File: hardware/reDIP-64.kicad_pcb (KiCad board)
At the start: 6 copper layers, 25.4 x 50.8 mm, 129 parts, among them J1 USB_C_Receptacle, J2 Conn_02x05_Odd_Even, J3 Conn_01x20, J4 Conn_01x20, J5 Conn_01x20, J6 Conn_01x20, J7 Conn_01x20, Q1 PDTA143ZMB, SW1 KXT331LHS, U1 FPF1048, U10 PTN5110, U11 FUSB340, U12 DSC1103CE2-135.0000, U13 FSA2259, U14 W957A8MFYA5I, U15 W25Q128JVPIM, U16 SN74CBTD16211DGVR, U17 SN74CBTD16211DGVR, U18 SN74CBTD16211DGVR, U19 SN74CBTD16211DGVR, U2 NCP163AMX250TBG, U3 MYRGP330100W21RA, U4 FPF2195, U5 NCP163AMX120TBG, U6 MYRGP120100W21RA, U7 NCP163AMX300TBG, U8 LFE5UM5G-25F-8MG285C, U9 SGTL5000XNLA3

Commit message: Various improvements
* Removed slash from sheet names
* Reannotated schematics
* Example derivation of clocks in schematics
* Identical capacitors for DisplayPort main lanes and AUX
* Replaced switch FSA2259UMX with FSUSB42UMX
* Modified PCB physical stackup to (hopefully) be manufacturable
* Only one microvia size (0.1mm)
* Changed track width for differential pairs
* Routing cleanups and improvements
* Added files for manufacture
* Updated README

Many thanks for advice and help go to @azonenberg, @DX-MON, @gatecat,
@smunaut, and @zyp.
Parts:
- removed the U13 at (108.8, 103.0)
- added U2: FSUSB42UMX, ONSemi:CASE523BC_1.4x1.8_P0.4mm, B.Cu at (108.8, 103.0)
- C1: renamed from C43; value 0.1uF -> 100nF
- C2: renamed from C45; value 0.1uF -> 100nF
- C3: renamed from C46; value 0.1uF -> 100nF
- C4: renamed from C47; value 0.1uF -> 100nF
- C5: renamed from C48; value 150nF -> 100nF
- C6: renamed from C49; value 150nF -> 100nF
- U3: renamed from U10; value PTN5110 -> PTN5110DHQ
- renumbered C41 to C10, C44 to C11, C7 to C12, C5 to C13, C21 to C14, C22 to C15, C23 to C16, C24 to C17, C6 to C18, C8 to C19, C25 to C20, C13 to C21, C26 to C22, C14 to C23, C27 to C24, C15 to C25, C28 to C26, C16 to C27, C17 to C28, C18 to C30, C30 to C31, C1 to C32, C9 to C33, C2 to C34, C10 to C35, C11 to C36, C3 to C37, C19 to C38, C12 to C39, C4 to C40, C20 to C41, C58 to C42, C62 to C43, C59 to C44, C63 to C45, C60 to C46, C64 to C47, C61 to C48, C65 to C49, C56 to C50, C66 to C51, C57 to C52, C67 to C53, C52 to C55, C55 to C56, C53 to C57, C50 to C58, C51 to C59, C31 to C60, C34 to C61, C35 to C62, C36 to C63, C32 to C64, C33 to C65, C37 to C66, C38 to C67, C42 to C7, C39 to C8, C40 to C9, D2 to D1, D3 to D2, D4 to D3, D1 to D4, FB3 to FB2, FB2 to FB3, J3 to J2, J6 to J3, J5 to J4, J7 to J5, J4 to J6, J2 to J7, R6 to R1, R13 to R10, R9 to R11, R14 to R12, R2 to R13, R3 to R14, R1 to R15, R21 to R17, R17 to R18, R22 to R19, R7 to R2, R19 to R20, R20 to R21, R18 to R22, R8 to R3, R10 to R4, R11 to R5, R4 to R6, R5 to R7, R12 to R8, R15 to R9, U11 to U1, U5 to U10, U2 to U11, U7 to U12, U16 to U13, U18 to U14, U17 to U15, U19 to U16, U14 to U17, U15 to U18, U9 to U19, U8 to U4, U12 to U5, U1 to U6, U4 to U7, U3 to U8, U6 to U9
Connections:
- net /Config / Memory/FLASH_~CS~ renamed /Config_Memory/FLASH_~CS~
- net /Config / Memory/LED renamed /Config_Memory/LED
- net /Config / Memory/MEM_CLK renamed /Config_Memory/MEM_CLK
- net /Config / Memory/MEM_IO0 renamed /Config_Memory/MEM_IO0
- net /Config / Memory/MEM_IO1 renamed /Config_Memory/MEM_IO1
- net /Config / Memory/MEM_IO2 renamed /Config_Memory/MEM_IO2
- net /Config / Memory/MEM_IO3 renamed /Config_Memory/MEM_IO3
- net /Config / Memory/MEM_IO4 renamed /Config_Memory/MEM_IO4
- net /Config / Memory/MEM_IO5 renamed /Config_Memory/MEM_IO5
- net /Config / Memory/MEM_IO6 renamed /Config_Memory/MEM_IO6
- net /Config / Memory/MEM_IO7 renamed /Config_Memory/MEM_IO7
- net /Config / Memory/RAM_~CS~ renamed /Config_Memory/RAM_~CS~
- net /Config / Memory/RWDS renamed /Config_Memory/RWDS
- net /Config / Memory/TCK renamed /Config_Memory/TCK
- net /Config / Memory/TDI renamed /Config_Memory/TDI
- net /Config / Memory/TDO renamed /Config_Memory/TDO
- net /Config / Memory/TMS renamed /Config_Memory/TMS
- net /Config / Memory/~BOOT~ renamed /Config_Memory/~BOOT~
- net /Config / Memory/~BTN~ renamed /Config_Memory/~BTN~
- net /FPGA / IO/A0 renamed /FPGA_IO/A0
- net /FPGA / IO/A1 renamed /FPGA_IO/A1
- net /FPGA / IO/A10 renamed /FPGA_IO/A10
- net /FPGA / IO/A11 renamed /FPGA_IO/A11
- net /FPGA / IO/A12 renamed /FPGA_IO/A12
- net /FPGA / IO/A13 renamed /FPGA_IO/A13
- net /FPGA / IO/A14 renamed /FPGA_IO/A14
- net /FPGA / IO/A15 renamed /FPGA_IO/A15
- net /FPGA / IO/A2 renamed /FPGA_IO/A2
- net /FPGA / IO/A3 renamed /FPGA_IO/A3
- net /FPGA / IO/A4 renamed /FPGA_IO/A4
- net /FPGA / IO/A5 renamed /FPGA_IO/A5
- net /FPGA / IO/A6 renamed /FPGA_IO/A6
- net /FPGA / IO/A7 renamed /FPGA_IO/A7
- net /FPGA / IO/A8 renamed /FPGA_IO/A8
- net /FPGA / IO/A9 renamed /FPGA_IO/A9
- net /FPGA / IO/AEC renamed /FPGA_IO/AEC
- net /FPGA / IO/BA renamed /FPGA_IO/BA
- net /FPGA / IO/CIA1_CNT renamed /FPGA_IO/CIA1_CNT
- net /FPGA / IO/CIA1_PA0 renamed /FPGA_IO/CIA1_PA0
- net /FPGA / IO/CIA1_PA1 renamed /FPGA_IO/CIA1_PA1
- net /FPGA / IO/CIA1_PA2 renamed /FPGA_IO/CIA1_PA2
- net /FPGA / IO/CIA1_PA3 renamed /FPGA_IO/CIA1_PA3
- net /FPGA / IO/CIA1_PA4 renamed /FPGA_IO/CIA1_PA4
- net /FPGA / IO/CIA1_PA5 renamed /FPGA_IO/CIA1_PA5
- net /FPGA / IO/CIA1_PA6 renamed /FPGA_IO/CIA1_PA6
- net /FPGA / IO/CIA1_PA7 renamed /FPGA_IO/CIA1_PA7
- net /FPGA / IO/CIA1_PB0 renamed /FPGA_IO/CIA1_PB0
- net /FPGA / IO/CIA1_PB1 renamed /FPGA_IO/CIA1_PB1
- net /FPGA / IO/CIA1_PB2 renamed /FPGA_IO/CIA1_PB2
- net /FPGA / IO/CIA1_PB3 renamed /FPGA_IO/CIA1_PB3
- net /FPGA / IO/CIA1_PB4 renamed /FPGA_IO/CIA1_PB4
- net /FPGA / IO/CIA1_PB5 renamed /FPGA_IO/CIA1_PB5
- net /FPGA / IO/CIA1_PB6 renamed /FPGA_IO/CIA1_PB6
- net /FPGA / IO/CIA1_PB7 renamed /FPGA_IO/CIA1_PB7
- net /FPGA / IO/CIA1_SP renamed /FPGA_IO/CIA1_SP
- net /FPGA / IO/CIA1_~FLAG~ renamed /FPGA_IO/CIA1_~FLAG~
- net /FPGA / IO/CIA1_~PC~_TOD renamed /FPGA_IO/CIA1_~PC~_TOD
- net /FPGA / IO/CIA2_CNT renamed /FPGA_IO/CIA2_CNT
- net /FPGA / IO/CIA2_PA0 renamed /FPGA_IO/CIA2_PA0
- net /FPGA / IO/CIA2_PA1 renamed /FPGA_IO/CIA2_PA1
- net /FPGA / IO/CIA2_PA2 renamed /FPGA_IO/CIA2_PA2
- net /FPGA / IO/CIA2_PA3 renamed /FPGA_IO/CIA2_PA3
- net /FPGA / IO/CIA2_PA4 renamed /FPGA_IO/CIA2_PA4
- net /FPGA / IO/CIA2_PA5 renamed /FPGA_IO/CIA2_PA5
- net /FPGA / IO/CIA2_PA6 renamed /FPGA_IO/CIA2_PA6
- net /FPGA / IO/CIA2_PA7 renamed /FPGA_IO/CIA2_PA7
- net /FPGA / IO/CIA2_PB0 renamed /FPGA_IO/CIA2_PB0
- net /FPGA / IO/CIA2_PB1 renamed /FPGA_IO/CIA2_PB1
- net /FPGA / IO/CIA2_PB2 renamed /FPGA_IO/CIA2_PB2
- net /FPGA / IO/CIA2_PB3 renamed /FPGA_IO/CIA2_PB3
- net /FPGA / IO/CIA2_PB4 renamed /FPGA_IO/CIA2_PB4
- net /FPGA / IO/CIA2_PB5 renamed /FPGA_IO/CIA2_PB5
- net /FPGA / IO/CIA2_PB6 renamed /FPGA_IO/CIA2_PB6
- net /FPGA / IO/CIA2_PB7 renamed /FPGA_IO/CIA2_PB7
- net /FPGA / IO/CIA2_SP renamed /FPGA_IO/CIA2_SP
- net /FPGA / IO/CIA2_~FLAG~ renamed /FPGA_IO/CIA2_~FLAG~
- net /FPGA / IO/CIA2_~PC~ renamed /FPGA_IO/CIA2_~PC~
- net /FPGA / IO/COLOR renamed /FPGA_IO/COLOR
- net /FPGA / IO/D0 renamed /FPGA_IO/D0
- net /FPGA / IO/D1 renamed /FPGA_IO/D1
- net /FPGA / IO/D2 renamed /FPGA_IO/D2
- net /FPGA / IO/D3 renamed /FPGA_IO/D3
- net /FPGA / IO/D4 renamed /FPGA_IO/D4
- net /FPGA / IO/D5 renamed /FPGA_IO/D5
- net /FPGA / IO/D6 renamed /FPGA_IO/D6
- net /FPGA / IO/D7 renamed /FPGA_IO/D7
- net /FPGA / IO/DOT_CLOCK renamed /FPGA_IO/DOT_CLOCK
- net /FPGA / IO/DP_AUX+ renamed /FPGA_IO/DP_AUX+
- net /FPGA / IO/DP_AUX- renamed /FPGA_IO/DP_AUX-
- net /FPGA / IO/I1_CNT renamed /FPGA_IO/I1_CNT
- net /FPGA / IO/I1_PA0 renamed /FPGA_IO/I1_PA0
- net /FPGA / IO/I1_PA1 renamed /FPGA_IO/I1_PA1
- net /FPGA / IO/I1_PA2 renamed /FPGA_IO/I1_PA2
- net /FPGA / IO/I1_PA3 renamed /FPGA_IO/I1_PA3
- net /FPGA / IO/I1_PA4 renamed /FPGA_IO/I1_PA4
- net /FPGA / IO/I1_PA5 renamed /FPGA_IO/I1_PA5
- net /FPGA / IO/I1_PA6 renamed /FPGA_IO/I1_PA6
- net /FPGA / IO/I1_PA7 renamed /FPGA_IO/I1_PA7
- net /FPGA / IO/I1_PB0 renamed /FPGA_IO/I1_PB0
- net /FPGA / IO/I1_PB1 renamed /FPGA_IO/I1_PB1
- net /FPGA / IO/I1_PB2 renamed /FPGA_IO/I1_PB2
- net /FPGA / IO/I1_PB3 renamed /FPGA_IO/I1_PB3
- net /FPGA / IO/I1_PB4 renamed /FPGA_IO/I1_PB4
- net /FPGA / IO/I1_PB5 renamed /FPGA_IO/I1_PB5
- net /FPGA / IO/I1_PB6 renamed /FPGA_IO/I1_PB6
- net /FPGA / IO/I1_PB7 renamed /FPGA_IO/I1_PB7
- net /FPGA / IO/I1_SP renamed /FPGA_IO/I1_SP
- net /FPGA / IO/I1_~FLAG~ renamed /FPGA_IO/I1_~FLAG~
- net /FPGA / IO/I1_~PC~_TOD renamed /FPGA_IO/I1_~PC~_TOD
- net /FPGA / IO/I2_CNT renamed /FPGA_IO/I2_CNT
- net /FPGA / IO/I2_PA0 renamed /FPGA_IO/I2_PA0
- net /FPGA / IO/I2_PA1 renamed /FPGA_IO/I2_PA1
- net /FPGA / IO/I2_PA2 renamed /FPGA_IO/I2_PA2
- net /FPGA / IO/I2_PA3 renamed /FPGA_IO/I2_PA3
- net /FPGA / IO/I2_PA4 renamed /FPGA_IO/I2_PA4
- net /FPGA / IO/I2_PA5 renamed /FPGA_IO/I2_PA5
- net /FPGA / IO/I2_PA6 renamed /FPGA_IO/I2_PA6
- net /FPGA / IO/I2_PA7 renamed /FPGA_IO/I2_PA7
- net /FPGA / IO/I2_PB0 renamed /FPGA_IO/I2_PB0
- net /FPGA / IO/I2_PB1 renamed /FPGA_IO/I2_PB1
- net /FPGA / IO/I2_PB2 renamed /FPGA_IO/I2_PB2
- net /FPGA / IO/I2_PB3 renamed /FPGA_IO/I2_PB3
- net /FPGA / IO/I2_PB4 renamed /FPGA_IO/I2_PB4
- net /FPGA / IO/I2_PB5 renamed /FPGA_IO/I2_PB5
- net /FPGA / IO/I2_PB6 renamed /FPGA_IO/I2_PB6
- net /FPGA / IO/I2_PB7 renamed /FPGA_IO/I2_PB7
- net /FPGA / IO/I2_SP renamed /FPGA_IO/I2_SP
- net /FPGA / IO/I2_~FLAG~ renamed /FPGA_IO/I2_~FLAG~
- net /FPGA / IO/I2_~PC~ renamed /FPGA_IO/I2_~PC~
- net /FPGA / IO/I_A0 renamed /FPGA_IO/I_A0
- net /FPGA / IO/I_A1 renamed /FPGA_IO/I_A1
- net /FPGA / IO/I_A10 renamed /FPGA_IO/I_A10
- net /FPGA / IO/I_A11 renamed /FPGA_IO/I_A11
- net /FPGA / IO/I_A12 renamed /FPGA_IO/I_A12
- net /FPGA / IO/I_A13 renamed /FPGA_IO/I_A13
- net /FPGA / IO/I_A14 renamed /FPGA_IO/I_A14
- net /FPGA / IO/I_A15 renamed /FPGA_IO/I_A15
- net /FPGA / IO/I_A2 renamed /FPGA_IO/I_A2
- net /FPGA / IO/I_A3 renamed /FPGA_IO/I_A3
- net /FPGA / IO/I_A4 renamed /FPGA_IO/I_A4
- net /FPGA / IO/I_A5 renamed /FPGA_IO/I_A5
- net /FPGA / IO/I_A6 renamed /FPGA_IO/I_A6
- net /FPGA / IO/I_A7 renamed /FPGA_IO/I_A7
- net /FPGA / IO/I_A8 renamed /FPGA_IO/I_A8
- net /FPGA / IO/I_A9 renamed /FPGA_IO/I_A9
- net /FPGA / IO/I_AEC renamed /FPGA_IO/I_AEC
- net /FPGA / IO/I_BA renamed /FPGA_IO/I_BA
- net /FPGA / IO/I_COLOR renamed /FPGA_IO/I_COLOR
- net /FPGA / IO/I_D0 renamed /FPGA_IO/I_D0
- net /FPGA / IO/I_D1 renamed /FPGA_IO/I_D1
- net /FPGA / IO/I_D2 renamed /FPGA_IO/I_D2
- net /FPGA / IO/I_D3 renamed /FPGA_IO/I_D3
- net /FPGA / IO/I_D4 renamed /FPGA_IO/I_D4
- net /FPGA / IO/I_D5 renamed /FPGA_IO/I_D5
- net /FPGA / IO/I_D6 renamed /FPGA_IO/I_D6
- net /FPGA / IO/I_D7 renamed /FPGA_IO/I_D7
- net /FPGA / IO/I_DOT_CLOCK renamed /FPGA_IO/I_DOT_CLOCK
- net /FPGA / IO/I_P0 renamed /FPGA_IO/I_P0
- net /FPGA / IO/I_P1 renamed /FPGA_IO/I_P1
- net /FPGA / IO/I_P2 renamed /FPGA_IO/I_P2
- net /FPGA / IO/I_P3 renamed /FPGA_IO/I_P3
- net /FPGA / IO/I_P4 renamed /FPGA_IO/I_P4
- net /FPGA / IO/I_P5 renamed /FPGA_IO/I_P5
- net /FPGA / IO/I_POT_X renamed /FPGA_IO/I_POT_X
- net /FPGA / IO/I_POT_Y renamed /FPGA_IO/I_POT_Y
- net /FPGA / IO/I_RDY renamed /FPGA_IO/I_RDY
- net /FPGA / IO/I_R_W renamed /FPGA_IO/I_R_W
- net /FPGA / IO/I_SYNC_LUM renamed /FPGA_IO/I_SYNC_LUM
- net /FPGA / IO/I_~DMA~ renamed /FPGA_IO/I_~DMA~
- net /FPGA / IO/I_~EXROM~ renamed /FPGA_IO/I_~EXROM~
- net /FPGA / IO/I_~GAME~ renamed /FPGA_IO/I_~GAME~
- net /FPGA / IO/I_~IO1~ renamed /FPGA_IO/I_~IO1~
- net /FPGA / IO/I_~IO2~ renamed /FPGA_IO/I_~IO2~
- net /FPGA / IO/I_~IRQ~ renamed /FPGA_IO/I_~IRQ~
- net /FPGA / IO/I_~MENU~ renamed /FPGA_IO/I_~MENU~
- net /FPGA / IO/I_~NMI~ renamed /FPGA_IO/I_~NMI~
- net /FPGA / IO/I_~RES~ renamed /FPGA_IO/I_~RES~
- net /FPGA / IO/I_~ROMH~ renamed /FPGA_IO/I_~ROMH~
- net /FPGA / IO/I_~ROML~ renamed /FPGA_IO/I_~ROML~
- net /FPGA / IO/I_Ø1_IN renamed /FPGA_IO/I_Ø1_IN
- net /FPGA / IO/I_Ø2_OUT renamed /FPGA_IO/I_Ø2_OUT
- net /FPGA / IO/P0 renamed /FPGA_IO/P0
- net /FPGA / IO/P1 renamed /FPGA_IO/P1
- net /FPGA / IO/P2 renamed /FPGA_IO/P2
- net /FPGA / IO/P3 renamed /FPGA_IO/P3
- net /FPGA / IO/P4 renamed /FPGA_IO/P4
- net /FPGA / IO/P5 renamed /FPGA_IO/P5
- net /FPGA / IO/POT_X renamed /FPGA_IO/POT_X
- net /FPGA / IO/POT_Y renamed /FPGA_IO/POT_Y
- net /FPGA / IO/RDY renamed /FPGA_IO/RDY
- net /FPGA / IO/R_W renamed /FPGA_IO/R_W
- net /FPGA / IO/SYNC_LUM renamed /FPGA_IO/SYNC_LUM
- net /FPGA / IO/USB_D+ renamed /FPGA_IO/USB_D+
- net /FPGA / IO/USB_D- renamed /FPGA_IO/USB_D-
- net /FPGA / IO/~ALERT~ renamed /FPGA_IO/~ALERT~
- net /FPGA / IO/~DMA~ renamed /FPGA_IO/~DMA~
- net /FPGA / IO/~EXROM~ renamed /FPGA_IO/~EXROM~
- net /FPGA / IO/~GAME~ renamed /FPGA_IO/~GAME~
- net /FPGA / IO/~IO1~ renamed /FPGA_IO/~IO1~
- net /FPGA / IO/~IO2~ renamed /FPGA_IO/~IO2~
- net /FPGA / IO/~IRQ~ renamed /FPGA_IO/~IRQ~
- net /FPGA / IO/~MENU~ renamed /FPGA_IO/~MENU~
- net /FPGA / IO/~NMI~ renamed /FPGA_IO/~NMI~
- net /FPGA / IO/~RES~ renamed /FPGA_IO/~RES~
- net /FPGA / IO/~ROMH~ renamed /FPGA_IO/~ROMH~
- net /FPGA / IO/~ROML~ renamed /FPGA_IO/~ROML~
- net /FPGA / IO/Ø1_IN renamed /FPGA_IO/Ø1_IN
- net /FPGA / IO/Ø2_OUT renamed /FPGA_IO/Ø2_OUT
- net /USB / DP/AUX+ renamed /USB_DisplayPort/AUX+
- net /USB / DP/AUX- renamed /USB_DisplayPort/AUX-
- net /USB / DP/CC1 renamed /USB_DisplayPort/CC1
- net /USB / DP/CC2 renamed /USB_DisplayPort/CC2
- net /USB / DP/CLK+ renamed /USB_DisplayPort/CLK+
- net /USB / DP/CLK- renamed /USB_DisplayPort/CLK-
- net /USB / DP/D+ renamed /USB_DisplayPort/D+
- net /USB / DP/D- renamed /USB_DisplayPort/D-
- net /USB / DP/DP0+ renamed /USB_DisplayPort/ML0+
- net /USB / DP/DP0- renamed /USB_DisplayPort/ML0-
- net /USB / DP/DP1+ renamed /USB_DisplayPort/ML1+
- net /USB / DP/DP1- renamed /USB_DisplayPort/ML1-
- net /USB / DP/RX+ renamed /USB_DisplayPort/RX+
- net /USB / DP/RX- renamed /USB_DisplayPort/RX-
- net /USB / DP/RX1+ renamed /USB_DisplayPort/RX1+
- net /USB / DP/RX1- renamed /USB_DisplayPort/RX1-
- net /USB / DP/RX2+ renamed /USB_DisplayPort/RX2+
- net /USB / DP/RX2- renamed /USB_DisplayPort/RX2-
- net /USB / DP/SBU1 renamed /USB_DisplayPort/SBU1
- net /USB / DP/SBU2 renamed /USB_DisplayPort/SBU2
- net /USB / DP/TX+ renamed /USB_DisplayPort/TX+
- net /USB / DP/TX- renamed /USB_DisplayPort/TX-
- net /USB / DP/TX1+ renamed /USB_DisplayPort/TX1+
- net /USB / DP/TX1- renamed /USB_DisplayPort/TX1-
- net /USB / DP/TX2+ renamed /USB_DisplayPort/TX2+
- net /USB / DP/TX2- renamed /USB_DisplayPort/TX2-
- net /USB / DP/USB_LINK renamed /USB_DisplayPort/USB_LINK
- net /USB / DP/USB_~CONN~ renamed /USB_DisplayPort/USB_~CONN~
- net /USB / DP/USB_~FLIP~ renamed /USB_DisplayPort/USB_~FLIP~
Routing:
- net GND: track 154.5 -> 160.7 mm, vias 231 -> 236
- net /USB_DisplayPort/SBU2: track 10.6 -> 6.06 mm, vias 4 -> 3
- net /USB_DisplayPort/USB_~FLIP~: track 17.2 -> 14.4 mm, vias 7 -> 6
- net /USB_DisplayPort/AUX-: track 31.3 -> 29.5 mm
- net /USB_DisplayPort/CC2: track 12.1 -> 10.4 mm
- net /USB_DisplayPort/SBU1: track 6.27 -> 4.72 mm
- net /Config_Memory/MEM_CLK: track 22.3 -> 23.7 mm
- net /USB_DisplayPort/RX1-: track 7.34 -> 6.03 mm
- net /USB_DisplayPort/RX2-: track 5.07 -> 3.77 mm
- net /USB_DisplayPort/AUX+: track 29.1 -> 30.3 mm
- net Net-(C35-Pad1): track 5.23 -> 4.30 mm
- net Net-(C34-Pad1): track 5.22 -> 4.29 mm
- net /USB_DisplayPort/TX2-: track 5.94 -> 5.07 mm
- net +3V3: track 80.5 -> 81.1 mm
- net /USB_DisplayPort/CC1: track 16.8 -> 16.2 mm
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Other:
- board text added: "21-06"
- board text added: "reDIP 64 R0.2"
- board text removed: "21-05"
- board text removed: "reDIP 64 R0.1"

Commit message: Added stitching vias and test points
Thanks to @azonenberg for help and suggestions.
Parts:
- added TP1: TestPoint, reDIP:TestPoint_Pad_D0.5mm, B.Cu at (110.4, 104.5)
- added TP2: TestPoint, reDIP:TestPoint_Pad_D0.5mm, B.Cu at (107.6, 128.7)
- added TP3: TestPoint, reDIP:TestPoint_Pad_D0.5mm, B.Cu at (109.6, 132.5)
- added TP4: TestPoint, reDIP:TestPoint_Pad_D0.5mm, B.Cu at (109.1, 131.6)
- added TP5: TestPoint, reDIP:TestPoint_Pad_D0.5mm, B.Cu at (103.0, 126.3)
- added TP6: TestPoint, reDIP:TestPoint_Pad_D0.5mm, B.Cu at (110.2, 131.6)
- added TP7: TestPoint, reDIP:TestPoint_Pad_D0.5mm, B.Cu at (110.4, 106.5)
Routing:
- net +3V3: track 81.1 -> 86.2 mm, vias 60 -> 67
- net VCCA: track 8.64 -> 12.6 mm, vias 6 -> 7
- net GND: track 160.7 -> 157.2 mm, vias 236 -> 264
- net +3V0: track 2.83 -> 4.68 mm
- net +1V2: track 51.6 -> 53.3 mm, vias 42 -> 46
- net +2V5: track 27.5 -> 28.0 mm, vias 15 -> 16
- net /USB_DisplayPort/TX-: track 18.4 -> 18.9 mm
- net /USB_DisplayPort/TX+: track 18.4 -> 18.9 mm
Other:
- board text added: "1V2"
- board text added: "2V5"
- board text added: "3V0"
- board text added: "GND"
- board text added: "VCCA"

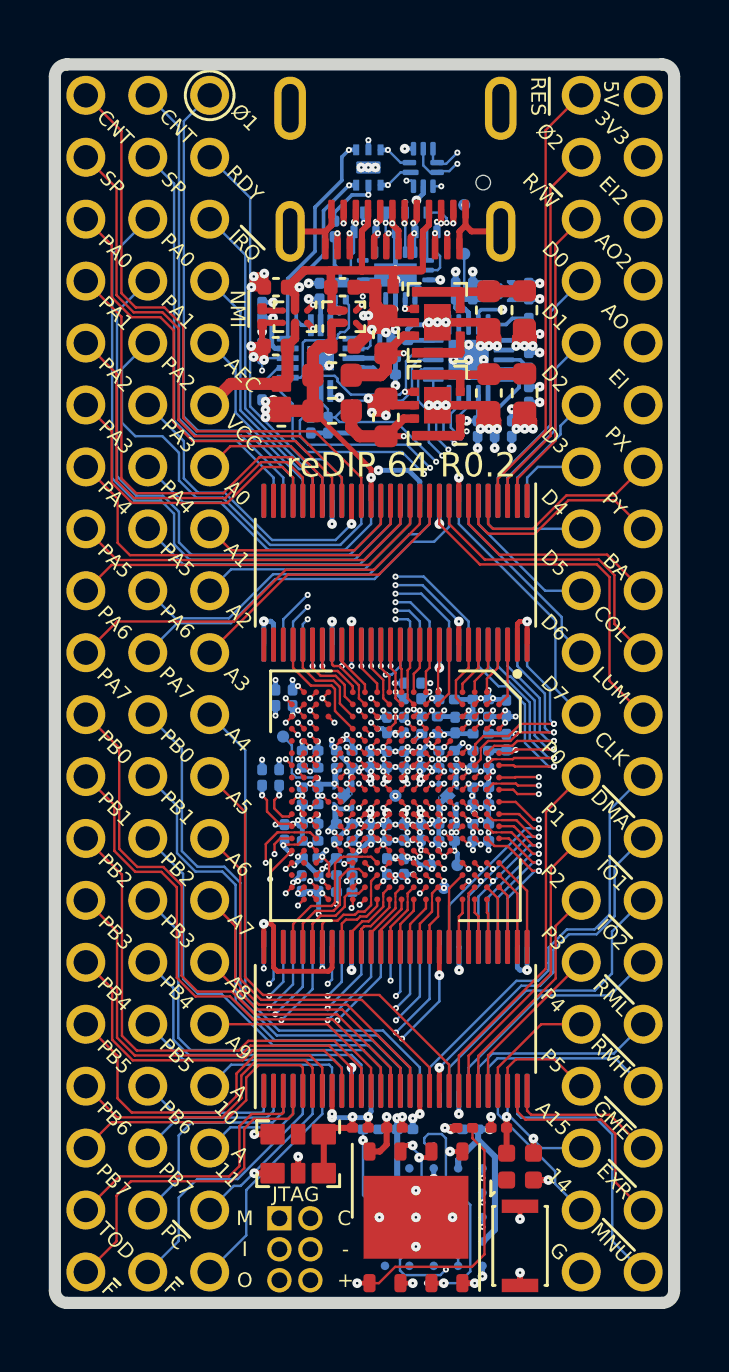
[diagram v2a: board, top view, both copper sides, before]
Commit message: Updated all KiCad files to current format
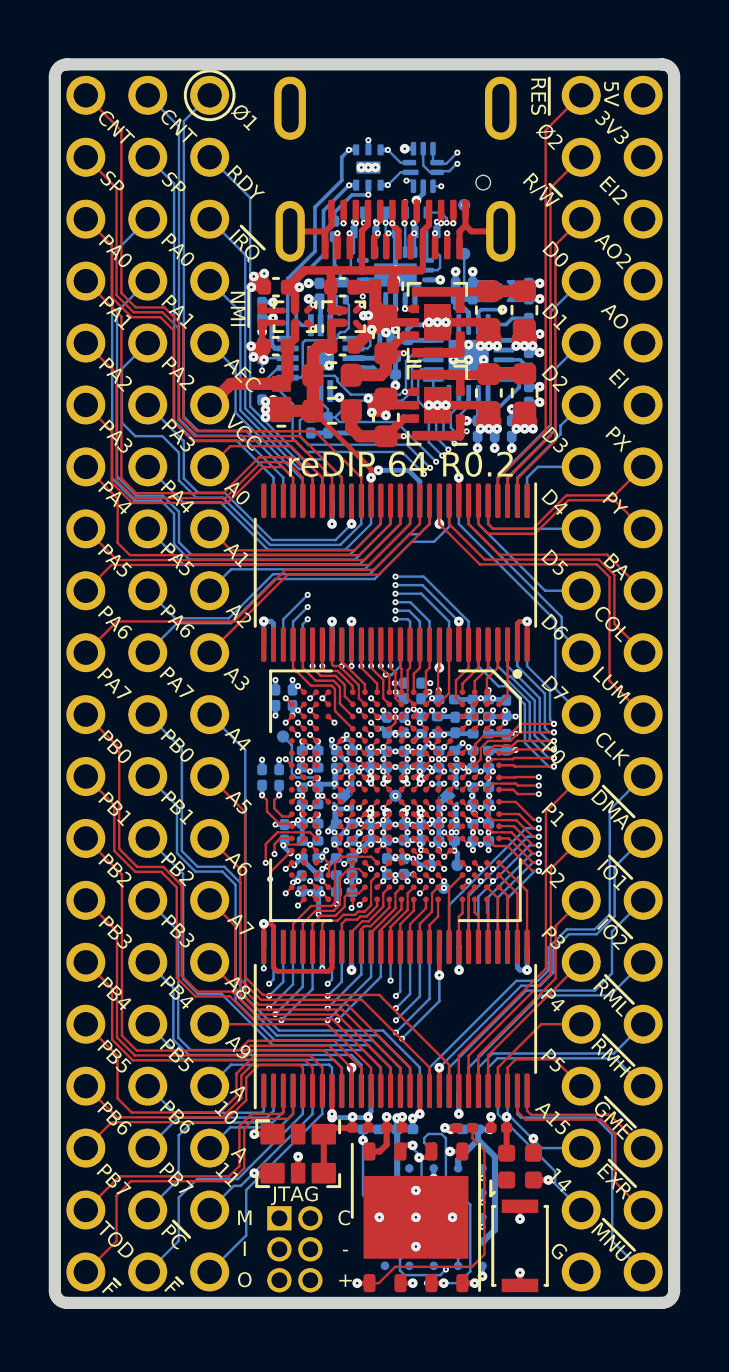
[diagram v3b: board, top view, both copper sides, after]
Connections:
- net /Config_Memory/FLASH_~CS~ renamed /Config_Memory/FLASH_~{CS}
- net /Config_Memory/RAM_~CS~ renamed /Config_Memory/RAM_~{CS}
- net /Config_Memory/~BOOT~ renamed /Config_Memory/~{BOOT}
- net /Config_Memory/~BTN~ renamed /Config_Memory/~{BTN}
- net /FPGA_IO/CIA1_~FLAG~ renamed /FPGA_IO/CIA1_~{FLAG}
- net /FPGA_IO/CIA1_~PC~_TOD renamed /FPGA_IO/CIA1_~{PC}_TOD
- net /FPGA_IO/CIA2_~FLAG~ renamed /FPGA_IO/CIA2_~{FLAG}
- net /FPGA_IO/CIA2_~PC~ renamed /FPGA_IO/CIA2_~{PC}
- net /FPGA_IO/I1_~FLAG~ renamed /FPGA_IO/I1_~{FLAG}
- net /FPGA_IO/I1_~PC~_TOD renamed /FPGA_IO/I1_~{PC}_TOD
- net /FPGA_IO/I2_~FLAG~ renamed /FPGA_IO/I2_~{FLAG}
- net /FPGA_IO/I2_~PC~ renamed /FPGA_IO/I2_~{PC}
- net /FPGA_IO/I_~DMA~ renamed /FPGA_IO/I_~{DMA}
- net /FPGA_IO/I_~EXROM~ renamed /FPGA_IO/I_~{EXROM}
- net /FPGA_IO/I_~GAME~ renamed /FPGA_IO/I_~{GAME}
- net /FPGA_IO/I_~IO1~ renamed /FPGA_IO/I_~{IO1}
- net /FPGA_IO/I_~IO2~ renamed /FPGA_IO/I_~{IO2}
- net /FPGA_IO/I_~IRQ~ renamed /FPGA_IO/I_~{IRQ}
- net /FPGA_IO/I_~MENU~ renamed /FPGA_IO/I_~{MENU}
- net /FPGA_IO/I_~NMI~ renamed /FPGA_IO/I_~{NMI}
- net /FPGA_IO/I_~RES~ renamed /FPGA_IO/I_~{RES}
- net /FPGA_IO/I_~ROMH~ renamed /FPGA_IO/I_~{ROMH}
- net /FPGA_IO/I_~ROML~ renamed /FPGA_IO/I_~{ROML}
- net /FPGA_IO/~ALERT~ renamed /FPGA_IO/~{ALERT}
- net /FPGA_IO/~DMA~ renamed /FPGA_IO/~{DMA}
- net /FPGA_IO/~EXROM~ renamed /FPGA_IO/~{EXROM}
- net /FPGA_IO/~GAME~ renamed /FPGA_IO/~{GAME}
- net /FPGA_IO/~IO1~ renamed /FPGA_IO/~{IO1}
- net /FPGA_IO/~IO2~ renamed /FPGA_IO/~{IO2}
- net /FPGA_IO/~IRQ~ renamed /FPGA_IO/~{IRQ}
- net /FPGA_IO/~MENU~ renamed /FPGA_IO/~{MENU}
- net /FPGA_IO/~NMI~ renamed /FPGA_IO/~{NMI}
- net /FPGA_IO/~RES~ renamed /FPGA_IO/~{RES}
- net /FPGA_IO/~ROMH~ renamed /FPGA_IO/~{ROMH}
- net /FPGA_IO/~ROML~ renamed /FPGA_IO/~{ROML}
- net /Power/~FAULT~ renamed /Power/~{FAULT}
- net /USB_DisplayPort/USB_~CONN~ renamed /USB_DisplayPort/USB_~{CONN}
- net /USB_DisplayPort/USB_~FLIP~ renamed /USB_DisplayPort/USB_~{FLIP}
- D5 pad 1: (no net) -> unconnected-(D5-Pad1)
- U13 pad 1: (no net) -> unconnected-(U13-Pad1)
- U13 pad 26: (no net) -> unconnected-(U13-Pad26)
- U13 pad 27: (no net) -> unconnected-(U13-Pad27)
- U13 pad 28: (no net) -> unconnected-(U13-Pad28)
- U13 pad 29: (no net) -> unconnected-(U13-Pad29)
- U13 pad 30: (no net) -> unconnected-(U13-Pad30)
- U13 pad 31: (no net) -> unconnected-(U13-Pad31)
- U14 pad 1: (no net) -> unconnected-(U14-Pad1)
- U14 pad 2: (no net) -> unconnected-(U14-Pad2)
- U14 pad 54: (no net) -> unconnected-(U14-Pad54)
- U15 pad 1: (no net) -> unconnected-(U15-Pad1)
- U16 pad 1: (no net) -> unconnected-(U16-Pad1)
- U17 pad A2: (no net) -> unconnected-(U17-PadA2)
- U17 pad A4: (no net) -> unconnected-(U17-PadA4)
- U17 pad A5: (no net) -> unconnected-(U17-PadA5)
- U17 pad B1: (no net) -> unconnected-(U17-PadB1)
- U17 pad B5: (no net) -> unconnected-(U17-PadB5)
- U17 pad C2: (no net) -> unconnected-(U17-PadC2)
- U17 pad C5: (no net) -> unconnected-(U17-PadC5)
- U19 pad 10: (no net) -> unconnected-(U19-Pad10)
- U19 pad 11: (no net) -> unconnected-(U19-Pad11)
- U19 pad 2: (no net) -> unconnected-(U19-Pad2)
- U19 pad 6: (no net) -> unconnected-(U19-Pad6)
- U19 pad 7: (no net) -> unconnected-(U19-Pad7)
- U3 pad 1: (no net) -> unconnected-(U3-Pad1)
- U3 pad 5: (no net) -> unconnected-(U3-Pad5)
- U4 pad U15: (no net) -> unconnected-(U4-PadU15)
- U4 pad V16: (no net) -> unconnected-(U4-PadV16)
- U4 pad V5: (no net) -> unconnected-(U4-PadV5)
- U4 pad V6: (no net) -> unconnected-(U4-PadV6)
- U4 pad V8: (no net) -> unconnected-(U4-PadV8)
- U4 pad V9: (no net) -> unconnected-(U4-PadV9)
- U5 pad 2: (no net) -> unconnected-(U5-Pad2)
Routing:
- net /FPGA_IO/D6: track 8.90 -> 8.14 mm
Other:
- board text added: "R/~{W}"
- board text added: "~{DMA}"
- board text added: "~{EXR}"
- board text added: "~{F}"
- board text added: "~{GME}"
- board text added: "~{IO1}"
- board text added: "~{IO2}"
- board text added: "~{IRQ}"
- board text added: "~{MNU}"
- board text added: "~{NMI}"
- board text added: "~{PC}"
- board text added: "~{RES}"
- board text added: "~{RMH}"
- board text added: "~{RML}"
- board text removed: "R/~W~"
- board text removed: "~DMA~"
- board text removed: "~EXR~"
- board text removed: "~F~"
- board text removed: "~GME~"
- board text removed: "~IO1~"
- board text removed: "~IO2~"
- board text removed: "~IRQ~"
- board text removed: "~MNU~"
- board text removed: "~NMI~"
- board text removed: "~PC~"
- board text removed: "~RES~"
- board text removed: "~RMH~"
- board text removed: "~RML~"
